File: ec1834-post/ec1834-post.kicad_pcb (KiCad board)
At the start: 2 copper layers, 100 x 75 mm, 11 parts, among them U0 BUS_EC1834_8Bit, U1 7432, U2 74HC04, U3 7430, U4 74HC374, U5 2732, U6 2732

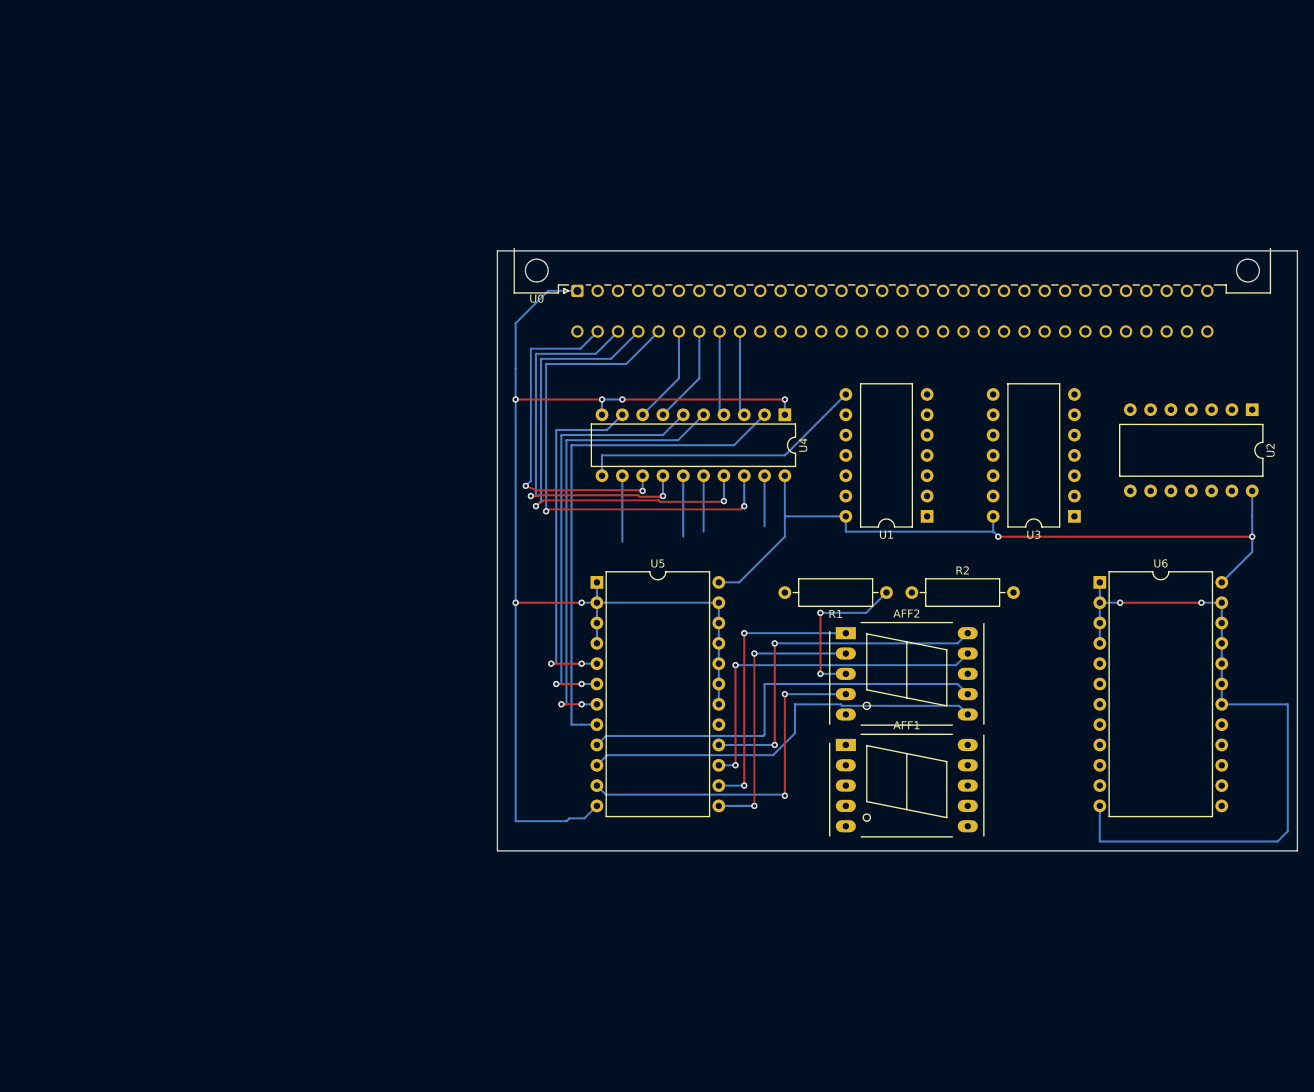
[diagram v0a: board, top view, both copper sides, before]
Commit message: Rework from CNC layout (which would be too close for 3018) to better layout for JLCPCB
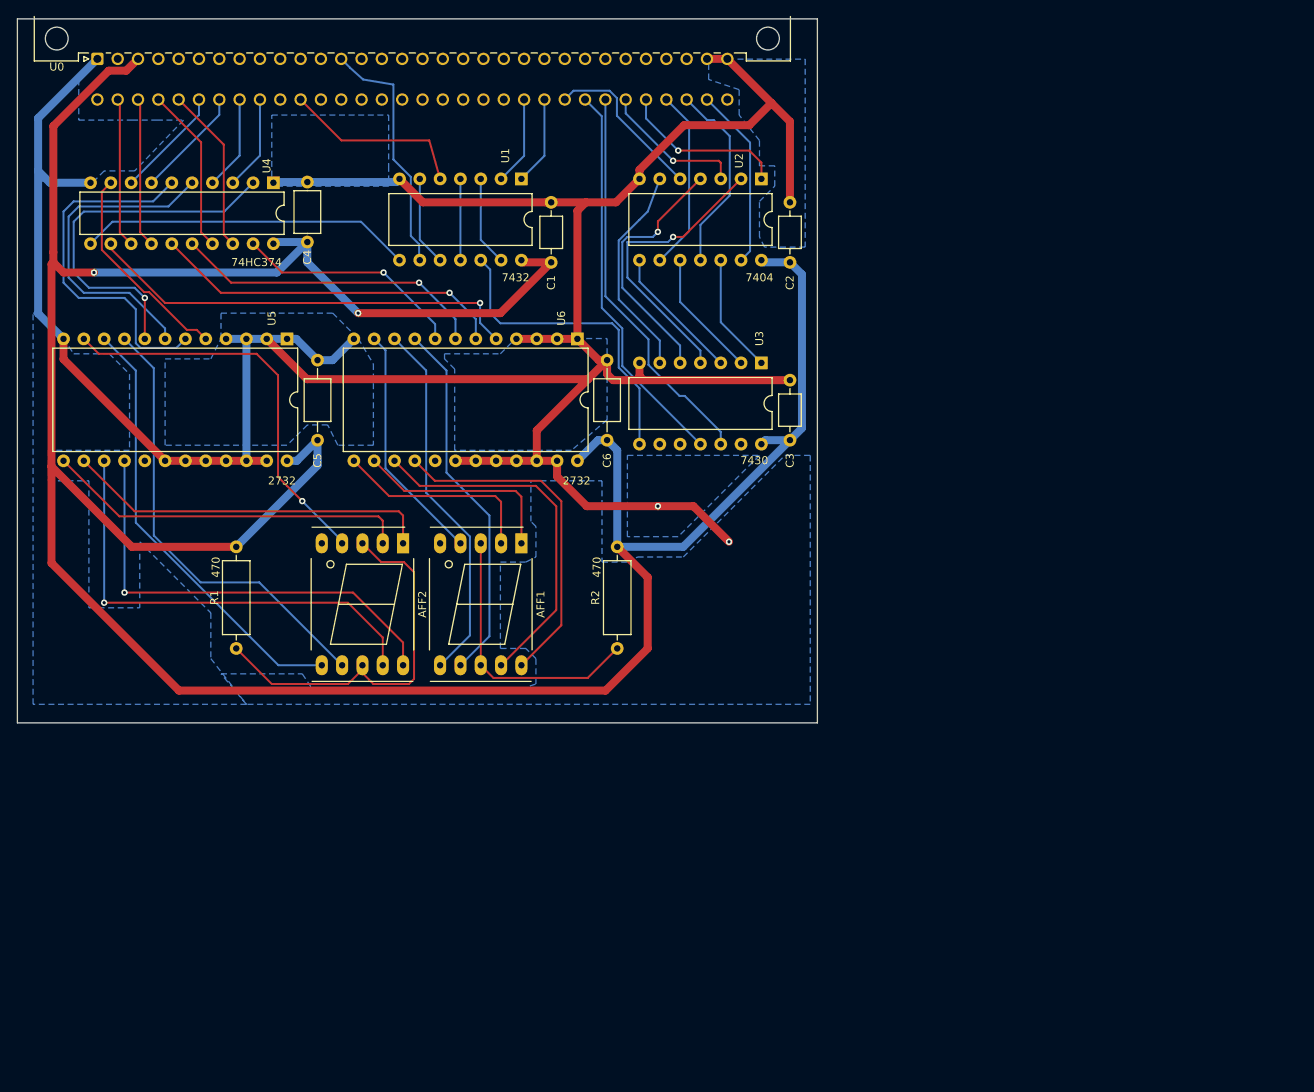
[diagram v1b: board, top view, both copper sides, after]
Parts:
- added C1: 100n, Capacitor_THT:C_Axial_L3.8mm_D2.6mm_P7.50mm_Horizontal, F.Cu at (85.7, 51.4)
- added C2: 100n, Capacitor_THT:C_Axial_L3.8mm_D2.6mm_P7.50mm_Horizontal, F.Cu at (115.6, 51.4)
- added C3: 100n, Capacitor_THT:C_Axial_L3.8mm_D2.6mm_P7.50mm_Horizontal, F.Cu at (115.6, 73.7)
- added C4: 100n, Capacitor_THT:C_Axial_L5.1mm_D3.1mm_P7.50mm_Horizontal, F.Cu at (55.2, 48.9)
- added C5: 100n, Capacitor_THT:C_Axial_L5.1mm_D3.1mm_P10.00mm_Horizontal, F.Cu at (56.5, 73.7)
- added C6: 100n, Capacitor_THT:C_Axial_L5.1mm_D3.1mm_P10.00mm_Horizontal, F.Cu at (92.7, 73.7)
- moved R1 81.6 mm to (46.4, 99.7), turned to 90 degrees
- moved U6 72.1 mm to (89.0, 61.0), turned to 270 degrees
- moved U4 70.2 mm to (51.0, 41.5)
- moved U2 67.8 mm to (112.0, 41.0)
- moved U0 66.6 mm to (29.0, 26.0)
- moved U1 66.0 mm to (82.0, 41.0), turned to 270 degrees
- moved AFF2 56.5 mm to (67.2, 86.6), turned to 270 degrees
- moved U5 49.3 mm to (52.7, 61.0), turned to 270 degrees
- moved AFF1 47.7 mm to (82.0, 86.6), turned to 270 degrees
- moved U3 43.6 mm to (112.0, 64.0), turned to 270 degrees
- moved R2 37.5 mm to (94.0, 99.7), turned to 90 degrees
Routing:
- net +5V: track 93.7 -> 373.0 mm
- net GND: track 253.9 -> 361.6 mm, vias 8 -> 2
- net A5: track 0.00 -> 49.4 mm
- net A6: track 0.00 -> 49.1 mm
- net Net-(U4-Pad12): track 8.25 -> 54.9 mm, vias 0 -> 1
- net Net-(AFF1-Pad6): track 0.00 -> 46.2 mm
- net Net-(AFF1-Pad7): track 0.00 -> 46.2 mm
- net Net-(AFF1-Pad9): track 0.00 -> 45.3 mm
- net Net-(AFF1-Pad10): track 0.00 -> 43.0 mm
- net D4: track 63.0 -> 20.8 mm, vias 2 -> 0
- net Net-(U1-Pad12): track 0.00 -> 39.4 mm
- net D5: track 59.3 -> 20.8 mm, vias 2 -> 0
- net Net-(U4-Pad15): track 7.62 -> 44.4 mm, vias 0 -> 1
- net Net-(U2-Pad2): track 0.00 -> 36.4 mm, vias 0 -> 1
- net Net-(AFF1-Pad3): track 0.00 -> 34.5 mm
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- added copper zone on B.Cu, net GND
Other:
- board size 100 x 75 mm -> 100 x 88 mm
- board text added: "2732"
- board text added: "470"
- board text added: "7404"
- board text added: "7430"
- board text added: "7432"
- board text added: "74HC374"

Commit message: New revision routing still in progress
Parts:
- removed AFF1, AFF2: LTS-6960HR, Display_7Segment:7SegmentLED_LTS6760_LTS6780
- added C7: 100uF 6,3V, Capacitor_THT:CP_Radial_D6.3mm_P2.50mm, F.Cu at (113.9, 35.8)
- added J-ADR: IO-ADDR, Connector_PinHeader_2.54mm:PinHeader_1x10_P2.54mm_Vertical, F.Cu at (87.5, 79.5)
- added J1: Bus_ISA_8bit, Connector_PCBEdge:ISA-8BIT-XT-IDE, F.Cu at (131.8, 66.0)
- added J2: Conn_02x07_Odd_Even, Connector_PinHeader_2.54mm:PinHeader_2x07_P2.54mm_Vertical, F.Cu at (25.9, 77.2)
- added J3: Conn_01x03, Connector_PinHeader_2.54mm:PinHeader_1x03_P2.54mm_Vertical, F.Cu at (23.4, 88.4)
- added J4: Conn_02x06_Odd_Even, Connector_PinHeader_2.54mm:PinHeader_2x06_P2.54mm_Vertical, F.Cu at (25.9, 52.8)
- added R3: 2K2, Resistor_THT:R_Axial_DIN0207_L6.3mm_D2.5mm_P7.62mm_Horizontal, F.Cu at (100.1, 52.6)
- added RN1: R_Network10, Resistor_THT:R_Array_SIP11, F.Cu at (94.0, 103.4)
- added SW1: SW_DIP_x10, Button_Switch_THT:SW_DIP_SPSTx10_Slide_9.78x27.58mm_W7.62mm_P2.54mm, F.Cu at (82.4, 79.5)
- added U7: SA39-11EWA, Display_7Segment:Sx39-1xxxxx, F.Cu at (58.7, 101.9)
- added U8: SA39-11EWA, Display_7Segment:Sx39-1xxxxx, F.Cu at (48.0, 101.9)
- C4: footprint Capacitor_THT:C_Axial_L5.1mm_D3.1mm_P7.50mm_Horizontal -> Capacitor_THT:C_Axial_L3.8mm_D2.6mm_P7.50mm_Horizontal
- C5, C6: footprint Capacitor_THT:C_Axial_L5.1mm_D3.1mm_P10.00mm_Horizontal -> Capacitor_THT:C_Axial_L3.8mm_D2.6mm_P7.50mm_Horizontal
- R1, R2: footprint Resistor_THT:R_Axial_DIN0309_L9.0mm_D3.2mm_P12.70mm_Horizontal -> Resistor_THT:R_Axial_DIN0207_L6.3mm_D2.5mm_P7.62mm_Horizontal
- U1: value 7432 -> 74LS688; footprint Package_DIP:DIP-14_W10.16mm -> Package_DIP:DIP-20_W7.62mm
- U2: value 74HC04 -> 74LS86; footprint Package_DIP:DIP-14_W10.16mm -> Package_DIP:DIP-14_W7.62mm
- U3: value 7430 -> 7432; footprint Package_DIP:DIP-14_W10.16mm -> Package_DIP:DIP-16_W7.62mm
- moved U6 55.8 mm to (35.6, 45.0), turned to 0 degrees
- moved C6 52.7 mm to (50.8, 41.7), turned to 180 degrees
- moved R2 47.0 mm to (48.4, 88.1), turned to 180 degrees
- moved C5 34.5 mm to (69.5, 41.7), turned to 180 degrees
- moved C1 27.7 mm to (111.7, 41.7), turned to 180 degrees
- moved C4 26.3 mm to (80.5, 41.7), turned to 180 degrees
- moved U3 23.1 mm to (104.0, 85.7), turned to 0 degrees
- moved U2 22.8 mm to (89.5, 45.0), turned to 0 degrees
- moved U1 22.4 mm to (104.0, 45.0), turned to 0 degrees
- moved U4 22.1 mm to (72.8, 45.0), turned to 0 degrees
- moved C2 20.8 mm to (97.2, 41.7), turned to 180 degrees
- moved R1 16.7 mm to (58.4, 88.1), turned to 180 degrees
- moved U5 16.1 mm to (54.2, 45.0), turned to 0 degrees
- moved C3 9.59 mm to (111.7, 82.4), turned to 180 degrees
- moved J0 0.77 mm to (29.7, 26.3)
- renumbered U0 to J0
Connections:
- net Net-(U4-Pad2) renamed /DB0
- net Net-(U4-Pad5) renamed /DB1
- net Net-(U4-Pad6) renamed /DB2
- net Net-(U4-Pad9) renamed /DB3
- J0 pad a14: Net-(U0-Pada14) -> IOR
- J0 pad a2: Net-(U0-Pada2) -> RESET
- J0 pad a20: Net-(U0-Pada20) -> CLK
- J0 pad a29: Net-(U0-Pada29) -> +5V
- J0 pad a5: Net-(U0-Pada5) -> -5V
- J0 pad a7: Net-(U0-Pada7) -> -12V
- J0 pad a9: Net-(U0-Pada9) -> +12V
- U1 pad 1: A8 -> AEN
- U1 pad 10: Net-(U1-Pad10) -> GND
- U1 pad 11: Net-(U1-Pad11) -> A4
- U1 pad 12: Net-(U1-Pad12) -> Net-(RN1-Pad7)
- U1 pad 13: Net-(U1-Pad13) -> A5
- U1 pad 14: +5V -> Net-(RN1-Pad6)
- U1 pad 2: A9 -> A0
- U1 pad 3: Net-(U1-Pad13) -> Net-(RN1-Pad11)
- U1 pad 4: Net-(U1-Pad11) -> A1
- U1 pad 5: AEN -> Net-(RN1-Pad10)
- U1 pad 6: Net-(U1-Pad10) -> A2
- U1 pad 7: GND -> Net-(RN1-Pad9)
- U1 pad 8: Net-(U1-Pad8) -> A3
- U1 pad 9: IOW -> Net-(RN1-Pad8)
- U2 pad 1: A3 -> A8
- U2 pad 10: Net-(U2-Pad10) -> Net-(R3-Pad1)
- U2 pad 11: A1 -> ENLATCH
- U2 pad 12: Net-(U2-Pad12) -> IOW
- U2 pad 13: A0 -> IOR
- U2 pad 2: Net-(U2-Pad2) -> /SW_A8
- U2 pad 3: A4 -> /SELA8
- U2 pad 4: Net-(U2-Pad4) -> A9
- U2 pad 5: A7 -> /SW_A9
- U2 pad 6: Net-(U2-Pad6) -> /SELA9
- U2 pad 9: A2 -> Net-(R3-Pad1)
- U3 pad 1: Net-(U2-Pad12) -> Net-(R3-Pad1)
- U3 pad 10: (no net) -> Net-(U3-Pad10)
- U3 pad 11: A6 -> Net-(U3-Pad11)
- U3 pad 12: A5 -> /SELA8
- U3 pad 13: (no net) -> /SELA9
- U3 pad 2: Net-(U2-Pad10) -> Net-(R3-Pad1)
- U3 pad 3: Net-(U2-Pad8) -> Net-(U3-Pad3)
- U3 pad 4: Net-(U2-Pad2) -> Net-(U3-Pad11)
- U3 pad 5: Net-(U2-Pad4) -> /SEL_AD
- U3 pad 6: Net-(U2-Pad6) -> Net-(U3-Pad10)
- U3 pad 8: Net-(U1-Pad12) -> Net-(U3-Pad8)
- U3 pad 9: (no net) -> ENLATCH
- U4 pad 11: Net-(U1-Pad8) -> Net-(U3-Pad8)
- U4 pad 12: Net-(U4-Pad12) -> /DB4
- U4 pad 15: Net-(U4-Pad15) -> /DB5
- U4 pad 16: Net-(U4-Pad16) -> /DB6
- U4 pad 19: Net-(U4-Pad19) -> /DB7
- U5 pad 20: GND -> IOWIOR
- U6 pad 20: GND -> IOWIOR
- U6 pad 5: Net-(U4-Pad12) -> /DB7
- U6 pad 6: Net-(U4-Pad15) -> /DB6
- U6 pad 7: Net-(U4-Pad16) -> /DB5
- U6 pad 8: Net-(U4-Pad19) -> /DB4
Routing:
- net GND: track 361.6 -> 15.9 mm, vias 2 -> 0
- net +5V: track 373.0 -> 178.9 mm, vias 2 -> 3
- net IOR: track 0.00 -> 141.0 mm, vias 0 -> 3
- net IOW: track 30.9 -> 150.7 mm, vias 0 -> 4
- net /SELA8: track 0.00 -> 98.6 mm, vias 0 -> 4
- net /SELA9: track 0.00 -> 88.3 mm, vias 0 -> 2
- net CLK: track 0.00 -> 87.7 mm, vias 0 -> 3
- net /SW_A8: track 0.00 -> 82.2 mm, vias 0 -> 2
- net IOWIOR: track 0.00 -> 71.4 mm, vias 0 -> 2
- net /SW_A9: track 0.00 -> 69.7 mm
- net /DB7: track 0.00 -> 69.5 mm
- net /DB5: track 0.00 -> 64.9 mm
- net D7: track 18.7 -> 82.6 mm, vias 0 -> 2
- net /DB6: track 0.00 -> 63.6 mm
- net /DB4: track 0.00 -> 62.1 mm
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- removed copper zone on B.Cu, net GND
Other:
- board size 100 x 88 mm -> 116.9 x 88 mm
- net class Default: clearance 0.2 -> 0.19; via_dia 0.8 -> 0.889; via_drill 0.4 -> 0.635
- rule trace_clearance: 0.2 -> 0.19
- rule via_min_drill: 0.3 -> 0.508
- rule via_min_size: 0.4 -> 0.889
- board text added: "Read"
- board text added: "Write"
- board text removed: "2732"
- board text removed: "470"
- board text removed: "7404"
- board text removed: "7430"
- board text removed: "7432"
- board text removed: "74HC374"

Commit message: Rebuild of PCB is done
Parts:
- added C8: 100n, Capacitor_THT:C_Axial_L3.8mm_D2.6mm_P7.50mm_Horizontal, F.Cu at (45.2, 49.9)
- added U9: 74HC374, Package_DIP:DIP-20_W7.62mm, F.Cu at (37.6, 53.9)
- C7: value 100uF 6,3V -> 100uF
- moved U5 46.5 mm to (64.9, 90.2)
- moved C5 45.8 mm to (80.1, 86.2)
- moved U6 30.7 mm to (64.9, 53.8)
- moved C6 30.5 mm to (80.1, 49.9)
- moved U4 24.3 mm to (50.2, 53.9)
- moved C4 24.2 mm to (57.8, 49.9)
- moved C3 22.6 mm to (118.9, 103.9), turned to 270 degrees
- moved J3 20.4 mm to (29.2, 108.0)
- moved J4 19.8 mm to (29.2, 72.4)
- moved R2 19.7 mm to (35.9, 103.4), turned to 0 degrees
- moved J2 18.3 mm to (29.2, 95.2)
- moved U8 16.6 mm to (43.4, 117.9)
- moved U7 16.6 mm to (54.4, 117.9)
- moved R1 15.8 mm to (54.2, 103.4)
- moved J-ADR 13.7 mm to (91.4, 92.6)
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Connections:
- J2 pad 1: /DB0 -> /J2D0
- J2 pad 2: /DB1 -> /J2D1
- J2 pad 3: /DB2 -> /J2D2
- J2 pad 4: /DB3 -> /J2D3
- J2 pad 5: /DB4 -> /J2D4
- J2 pad 6: /DB5 -> /J2D5
- J2 pad 7: /DB6 -> /J2D6
- J2 pad 8: /DB7 -> /J2D7
- U3 pad 1: Net-(R3-Pad1) -> Net-(U3-Pad1)
- U3 pad 2: Net-(R3-Pad1) -> IOWIOR
- U3 pad 8: Net-(U3-Pad8) -> Net-(U3-Pad1)
- U4 pad 11: Net-(U3-Pad8) -> Net-(U3-Pad3)
- U5 pad 20: IOWIOR -> GND
- U6 pad 20: IOWIOR -> GND
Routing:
- net +5V: track 178.9 -> 576.6 mm, vias 3 -> 22
- net Net-(U3-Pad1): track 0.00 -> 153.1 mm, vias 0 -> 4
- net RESET: track 51.9 -> 194.1 mm, vias 0 -> 2
- net CLK: track 87.7 -> 218.5 mm, vias 3 -> 5
- net -5V: track 38.6 -> 166.7 mm, vias 0 -> 4
- net -12V: track 42.2 -> 169.7 mm, vias 0 -> 4
- net +12V: track 53.5 -> 180.2 mm, vias 0 -> 3
- net Net-(U3-Pad3): track 0.00 -> 114.2 mm, vias 0 -> 3
- net D0: track 44.9 -> 127.7 mm, vias 1 -> 4
- net D7: track 82.6 -> 164.6 mm, vias 2 -> 6
- net A0: track 19.3 -> 98.6 mm, vias 2 -> 4
- net IOR: track 141.0 -> 220.2 mm, vias 3 -> 9
- net D2: track 62.6 -> 141.4 mm, vias 1 -> 5
- net D1: track 51.4 -> 128.7 mm, vias 1 -> 5
- net IOW: track 150.7 -> 227.8 mm, vias 4 -> 7
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- added copper zone on B.Cu, net GND
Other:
- board size 116.9 x 88 mm -> 116.9 x 103.7 mm
